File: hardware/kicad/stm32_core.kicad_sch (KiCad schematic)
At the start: 18 parts, among them J201 SWD, U201 STM32F405RGT6, Y201 8MHz

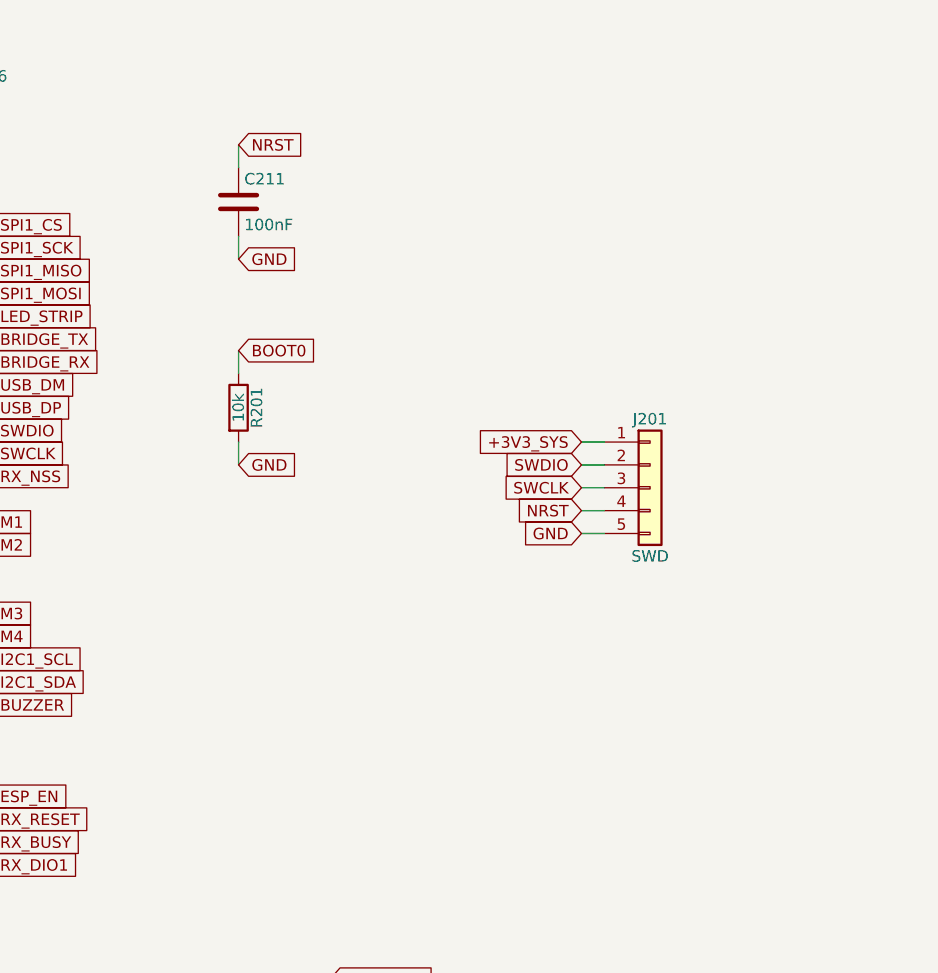
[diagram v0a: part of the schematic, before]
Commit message: Block 5: ESP32 sheet, mode switch, UART bridge, flash lines; PB12 series R; Block 1 GND to power symbols
Co-Authored-By: Claude Sonnet 5 <noreply@anthropic.com>
Claude-Session: https://claude.ai/code/session_01JDQYoFvbjRHNSgGtfc2pWo
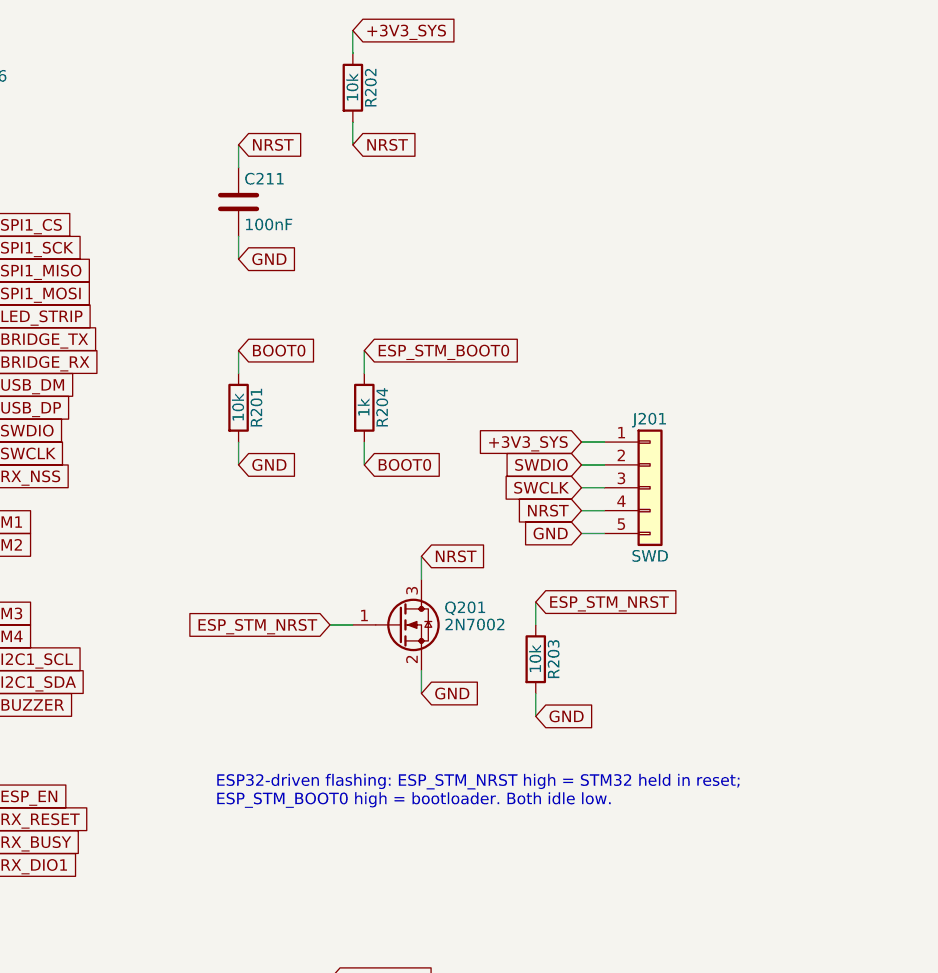
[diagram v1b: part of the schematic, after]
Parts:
- added Q201: 2N7002, Package_TO_SOT_SMD:SOT-23, symbol Transistor_FET:Q_NMOS_GSD
- added R202, R203: 10k, Resistor_SMD:R_0603_1608Metric, symbol Device:R
- added R204: 1k, Resistor_SMD:R_0603_1608Metric, symbol Device:R
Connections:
- net +3V3_SYS: now also R202.1
- net BOOT0: now also R204.2
- net GND: now also Q201.2 (S), R203.2
- net NRST: now also Q201.3 (D), R202.2
- new net ESP_STM_BOOT0: R204.1
- new net ESP_STM_NRST: Q201.1 (G), R203.1
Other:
- note added: "ESP32-driven flashing: ESP_STM_NRST high = STM32 held in reset; ESP_STM_BOOT0 high = bootloader. Both idle low."

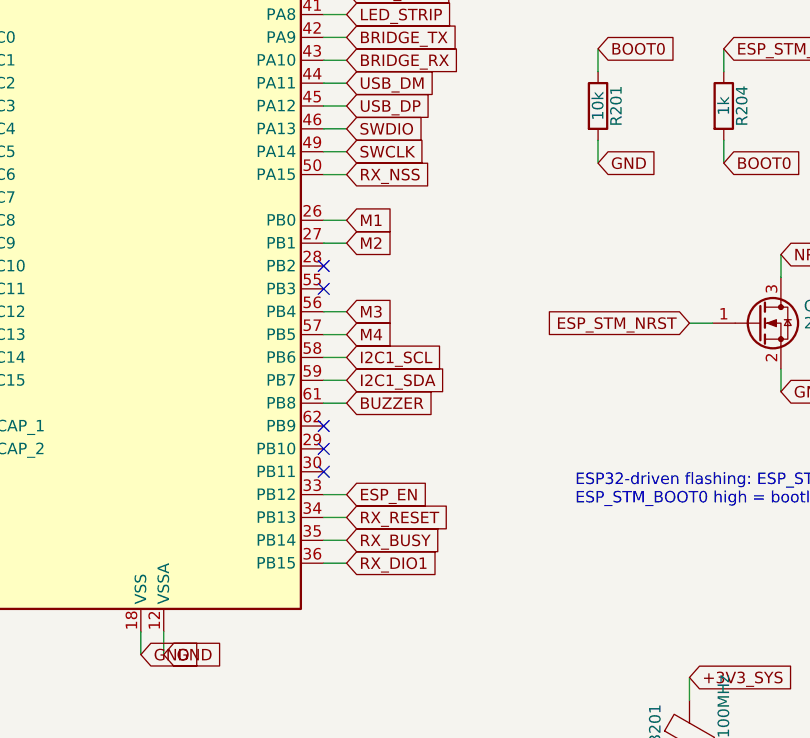
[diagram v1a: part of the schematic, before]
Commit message: Apply SPI-ELRS removal: FLASH_CS=PA15, RX_UART on PB10/PB11, PB13-15 spare
Co-Authored-By: Claude Sonnet 5 <noreply@anthropic.com>
Claude-Session: https://claude.ai/code/session_01JDQYoFvbjRHNSgGtfc2pWo
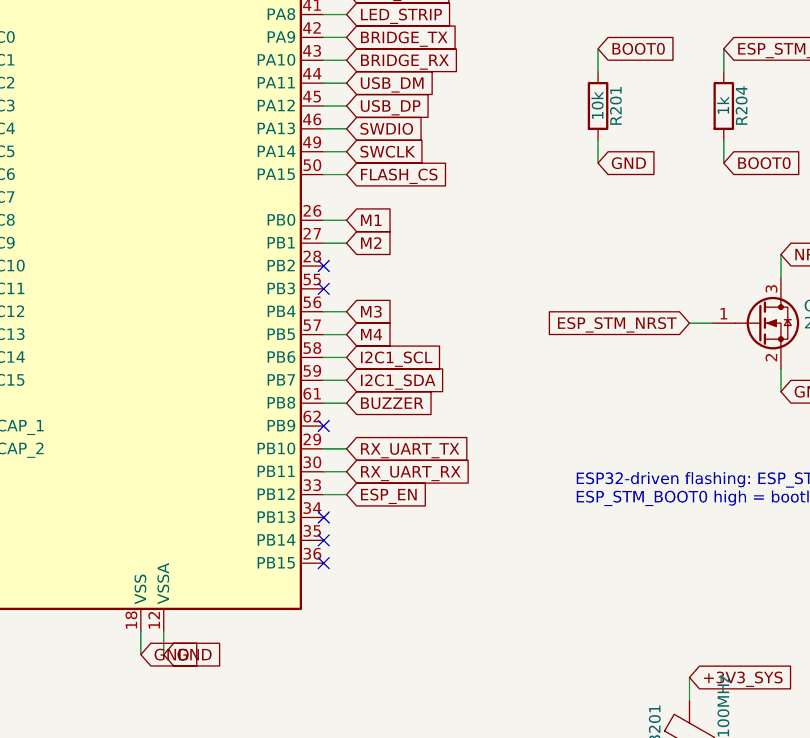
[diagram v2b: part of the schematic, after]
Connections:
- net RX_UART_TX: now reaches U201.29 (PB10)
- net RX_UART_RX: now reaches U201.30 (PB11)
- net RX_BUSY: no longer names the net of U201.35 (PB14)
- net RX_DIO1: no longer names the net of U201.36 (PB15)
- net RX_NSS renamed FLASH_CS
- net RX_RESET: no longer names the net of U201.34 (PB13)
- no-connect marks 19 -> 20
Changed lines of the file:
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@@
-	)
-	(no_connect
-		(at 210.82 179.07)
-	)
-	(no_connect
-		(at 210.82 181.61)
 	)
 	(no_connect
@@
 		(at 210.82 176.53)
 	)
+	(no_connect
+		(at 210.82 186.69)
+	)
+	(no_connect
+		(at 210.82 189.23)
+	)
+	(no_connect
+		(at 210.82 191.77)
+	)
 	(wire
 		(pts
@@
 	(wire
 		(pts
-			(xy 210.82 186.69)
-			(xy 213.36 186.69)
-		)
-	)
-	(wire
-		(pts
-			(xy 210.82 189.23)
-			(xy 213.36 189.23)
-		)
-	)
-	(wire
-		(pts
-			(xy 210.82 191.77)
-			(xy 213.36 191.77)
-		)
-	)
-	(wire
-		(pts
 			(xy 210.82 130.81)
 			(xy 213.36 130.81)
@@
 		)
 	)
+	(wire
+		(pts
+			(xy 210.82 179.07)
+			(xy 213.36 179.07)
+		)
+	)
+	(wire
+		(pts
+			(xy 210.82 181.61)
+			(xy 213.36 181.61)
+		)
+	)
+	(text "ESP32-driven flashing: ESP_STM_NRST high = STM32 held in reset;\nESP_STM_BOOT0 high = bootloader. Both idle low."
+		(at 238.76 185.42 0)
+		(effects
+			(font
+				(size 1.27 1.27)
+			)
+			(justify left bottom)
+		)
+	)
 	(label "VDDA"
 		(at 198.12 100.33 0)
@@
 		)
 	)
-	(global_label "RX_RESET"
-		(shape input)
-		(at 213.36 186.69 0)
-		(effects
-			(font
-				(size 1.27 1.27)
-			)
-			(justify left)
-		)
-	)
-	(global_label "RX_BUSY"
-		(shape input)
-		(at 213.36 189.23 0)
-		(effects
-			(font
-				(size 1.27 1.27)
-			)
-			(justify left)
-		)
-	)
-	(global_label "RX_DIO1"
-		(shape input)
-		(at 213.36 191.77 0)
-		(effects
-			(font
-				(size 1.27 1.27)
-			)
-			(justify left)
-		)
-	)
 	(global_label "LED_STRIP"
 		(shape input)
@@
 		)
 	)
-	(global_label "RX_NSS"
+	(global_label "M3"
+		(shape input)
+		(at 213.36 163.83 0)
+		(effects
+			(font
+				(size 1.27 1.27)
+			)
+			(justify left)
+		)
+	)
+	(global_label "M4"
+		(shape input)
+		(at 213.36 166.37 0)
+		(effects
+			(font
+				(size 1.27 1.27)
+			)
+			(justify left)
+		)
+	)
+	(global_label "I2C1_SCL"
+		(shape input)
+		(at 213.36 168.91 0)
+		(effects
+			(font
+				(size 1.27 1.27)
+			)
+			(justify left)
+		)
+	)
+	(global_label "I2C1_SDA"
+		(shape input)
+		(at 213.36 171.45 0)
+		(effects
+			(font
+				(size 1.27 1.27)
+			)
+			(justify left)
+		)
+	)
+	(global_label "BUZZER"
+		(shape input)
+		(at 213.36 173.99 0)
+		(effects
+			(font
+				(size 1.27 1.27)
+			)
+			(justify left)
+		)
+	)
+	(global_label "+3V3_SYS"
+		(shape input)
+		(at 254 99.06 0)
+		(effects
+			(font
+				(size 1.27 1.27)
+			)
+			(justify left)
+		)
+	)
+	(global_label "NRST"
+		(shape input)
+		(at 254 111.76 0)
+		(effects
+			(font
+				(size 1.27 1.27)
+			)
+			(justify left)
+		)
+	)
+	(global_label "ESP_STM_BOOT0"
+		(shape input)
+		(at 255.27 134.62 0)
+		(effects
+			(font
+				(size 1.27 1.27)
+			)
+			(justify left)
+		)
+	)
+	(global_label "BOOT0"
+		(shape input)
+		(at 255.27 147.32 0)
+		(effects
+			(font
+				(size 1.27 1.27)
+			)
+			(justify left)
+		)
+	)
+	(global_label "NRST"
+		(shape input)
+		(at 261.62 157.48 0)
+		(effects
+			(font
+				(size 1.27 1.27)
+			)
+			(justify left)
+		)
+	)
+	(global_label "GND"
+		(shape input)
+		(at 261.62 172.72 0)
+		(effects
+			(font
+				(size 1.27 1.27)
+			)
+			(justify left)
+		)
+	)
+	(global_label "ESP_STM_NRST"
+		(shape input)
+		(at 251.46 165.1 180)
+		(effects
+			(font
+				(size 1.27 1.27)
+			)
+			(justify right)
+		)
+	)
+	(global_label "ESP_STM_NRST"
+		(shape input)
+		(at 274.32 162.56 0)
+		(effects
+			(font
+				(size 1.27 1.27)
+			)
+			(justify left)
+		)
+	)
+	(global_label "GND"
+		(shape input)
+		(at 274.32 175.26 0)
+		(effects
+			(font
+				(size 1.27 1.27)
+			)
+			(justify left)
+		)
+	)
+	(global_label "FLASH_CS"
 		(shape input)
 		(at 213.36 148.59 0)
@@
 		)
 	)
-	(global_label "M3"
-		(shape input)
-		(at 213.36 163.83 0)
-		(effects
-			(font
-				(size 1.27 1.27)
-			)
-			(justify left)
-		)
-	)
-	(global_label "M4"
-		(shape input)
-		(at 213.36 166.37 0)
-		(effects
-			(font
-				(size 1.27 1.27)
-			)
-			(justify left)
-		)
-	)
-	(global_label "I2C1_SCL"
-		(shape input)
-		(at 213.36 168.91 0)
-		(effects
-			(font
-				(size 1.27 1.27)
-			)
-			(justify left)
-		)
-	)
-	(global_label "I2C1_SDA"
-		(shape input)
-		(at 213.36 171.45 0)
-		(effects
-			(font
-				(size 1.27 1.27)
-			)
-			(justify left)
-		)
-	)
-	(global_label "BUZZER"
-		(shape input)
-		(at 213.36 173.99 0)
-		(effects
-			(font
-				(size 1.27 1.27)
-			)
-			(justify left)
-		)
-	)
-	(global_label "+3V3_SYS"
-		(shape input)
-		(at 254 99.06 0)
-		(effects
-			(font
-				(size 1.27 1.27)
-			)
-			(justify left)
-		)
-	)
-	(global_label "NRST"
-		(shape input)
-		(at 254 111.76 0)
-		(effects
-			(font
-				(size 1.27 1.27)
-			)
-			(justify left)
-		)
-	)
-	(global_label "ESP_STM_BOOT0"
-		(shape input)
-		(at 255.27 134.62 0)
-		(effects
-			(font
-				(size 1.27 1.27)
-			)
-			(justify left)
-		)
-	)
-	(global_label "BOOT0"
-		(shape input)
-		(at 255.27 147.32 0)
-		(effects
-			(font
-				(size 1.27 1.27)
-			)
-			(justify left)
-		)
-	)
-	(global_label "NRST"
-		(shape input)
-		(at 261.62 157.48 0)
-		(effects
-			(font
-				(size 1.27 1.27)
-			)
-			(justify left)
-		)
-	)
-	(global_label "GND"
-		(shape input)
-		(at 261.62 172.72 0)
-		(effects
-			(font
-				(size 1.27 1.27)
-			)
-			(justify left)
-		)
-	)
-	(global_label "ESP_STM_NRST"
-		(shape input)
-		(at 251.46 165.1 180)
-		(effects
-			(font
-				(size 1.27 1.27)
-			)
-			(justify right)
-		)
-	)
-	(global_label "ESP_STM_NRST"
-		(shape input)
-		(at 274.32 162.56 0)
-		(effects
-			(font
-				(size 1.27 1.27)
-			)
-			(justify left)
-		)
-	)
-	(global_label "GND"
-		(shape input)
-		(at 274.32 175.26 0)
-		(effects
-			(font
-				(size 1.27 1.27)
-			)
-			(justify left)
-		)
-	)
-  (text "ESP32-driven flashing: ESP_STM_NRST high = STM32 held in reset;\nESP_STM_BOOT0 high = bootloader. Both idle low."
-    (at 238.76 185.42 0)
-    (effects (font (size 1.27 1.27)) (justify left bottom))
-  )
+	(global_label "RX_UART_TX"
+		(shape input)
+		(at 213.36 179.07 0)
+		(effects
+			(font
+				(size 1.27 1.27)
+			)
+			(justify left)
+		)
+	)
+	(global_label "RX_UART_RX"
+		(shape input)
+		(at 213.36 181.61 0)
+		(effects
+			(font
+				(size 1.27 1.27)
+			)
+			(justify left)
+		)
+	)
 	(symbol
 		(lib_id "MCU_ST_STM32F4:STM32F405RGTx")

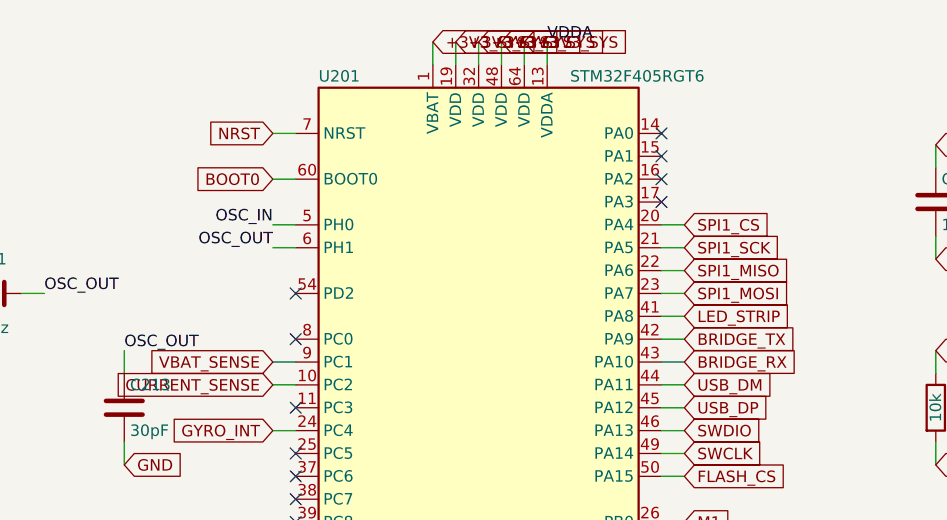
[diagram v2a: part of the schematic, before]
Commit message: Block 7: expansion connectors (RC, GPS, aux I2C, buzzer, LED)
- J701 CRSF on USART3, J702 GPS on USART2 (PA2/PA3)
- ESC_TLM assigned to UART5_RX (PD2), preserving USART2/4/6 as full pairs
- Buzzer low-side 2N7002 with flyback clamp; LED strip via 330R series
- Removes no-connect flags on PA2/PA3/PD2 in stm32_core
- LED_DATA drives WS2812 at 3V3 (VIH marginal) - see sheet note

Co-Authored-By: Claude Sonnet 5 <noreply@anthropic.com>
Claude-Session: https://claude.ai/code/session_0171uwNh8K8uwZuWio9f35u1
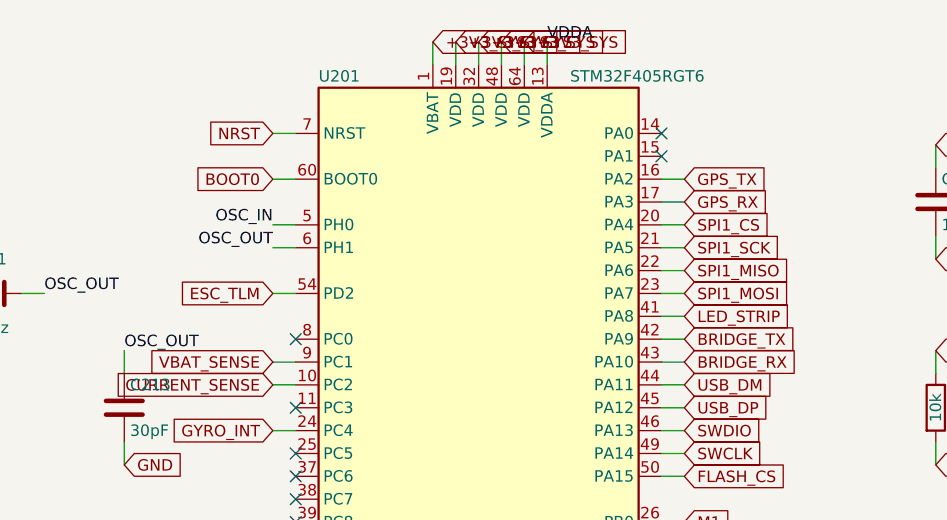
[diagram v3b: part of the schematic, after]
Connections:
- net GPS_TX: now reaches U201.16 (PA2)
- net GPS_RX: now reaches U201.17 (PA3)
- net ESC_TLM: now reaches U201.54 (PD2)
- no-connect marks 20 -> 17
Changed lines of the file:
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@@
-	)
-	(no_connect
-		(at 210.82 115.57)
-	)
-	(no_connect
-		(at 210.82 118.11)
 	)
 	(no_connect
@@
 	)
 	(no_connect
-		(at 170.18 128.27)
-	)
-	(no_connect
 		(at 210.82 161.29)
 	)
@@
 		)
 	)
+	(wire
+		(pts
+			(xy 210.82 115.57)
+			(xy 213.36 115.57)
+		)
+	)
+	(wire
+		(pts
+			(xy 210.82 118.11)
+			(xy 213.36 118.11)
+		)
+	)
+	(wire
+		(pts
+			(xy 170.18 128.27)
+			(xy 167.64 128.27)
+		)
+	)
 	(text "ESP32-driven flashing: ESP_STM_NRST high = STM32 held in reset;\nESP_STM_BOOT0 high = bootloader. Both idle low."
 		(at 238.76 185.42 0)
@@
 		)
 	)
+	(global_label "GPS_TX"
+		(shape input)
+		(at 213.36 115.57 0)
+		(effects
+			(font
+				(size 1.27 1.27)
+			)
+			(justify left)
+		)
+	)
+	(global_label "GPS_RX"
+		(shape input)
+		(at 213.36 118.11 0)
+		(effects
+			(font
+				(size 1.27 1.27)
+			)
+			(justify left)
+		)
+	)
+	(global_label "ESC_TLM"
+		(shape input)
+		(at 167.64 128.27 180)
+		(effects
+			(font
+				(size 1.27 1.27)
+			)
+			(justify right)
+		)
+	)
